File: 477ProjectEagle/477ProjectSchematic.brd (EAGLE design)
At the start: 100 x 80 mm, 49 parts, among them Q1 AO4419, X10 22-23-2041, X9 22-23-2041

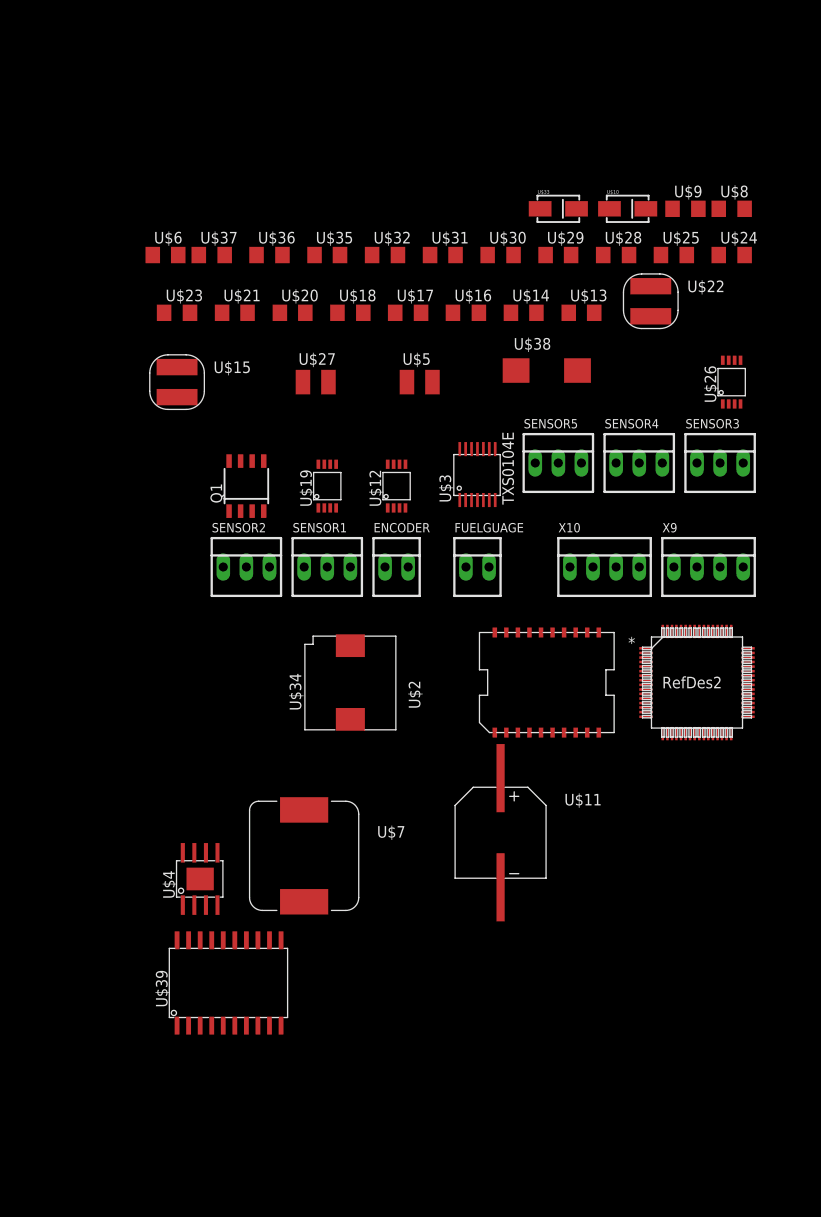
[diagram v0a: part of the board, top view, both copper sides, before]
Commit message: Updated micro code and small schematic fix
Added ADC code to micro project. The code initializes adc to capture
data from all 5 sensors the interrupt when done.
Also added decoupling caps to the ADC input lines.
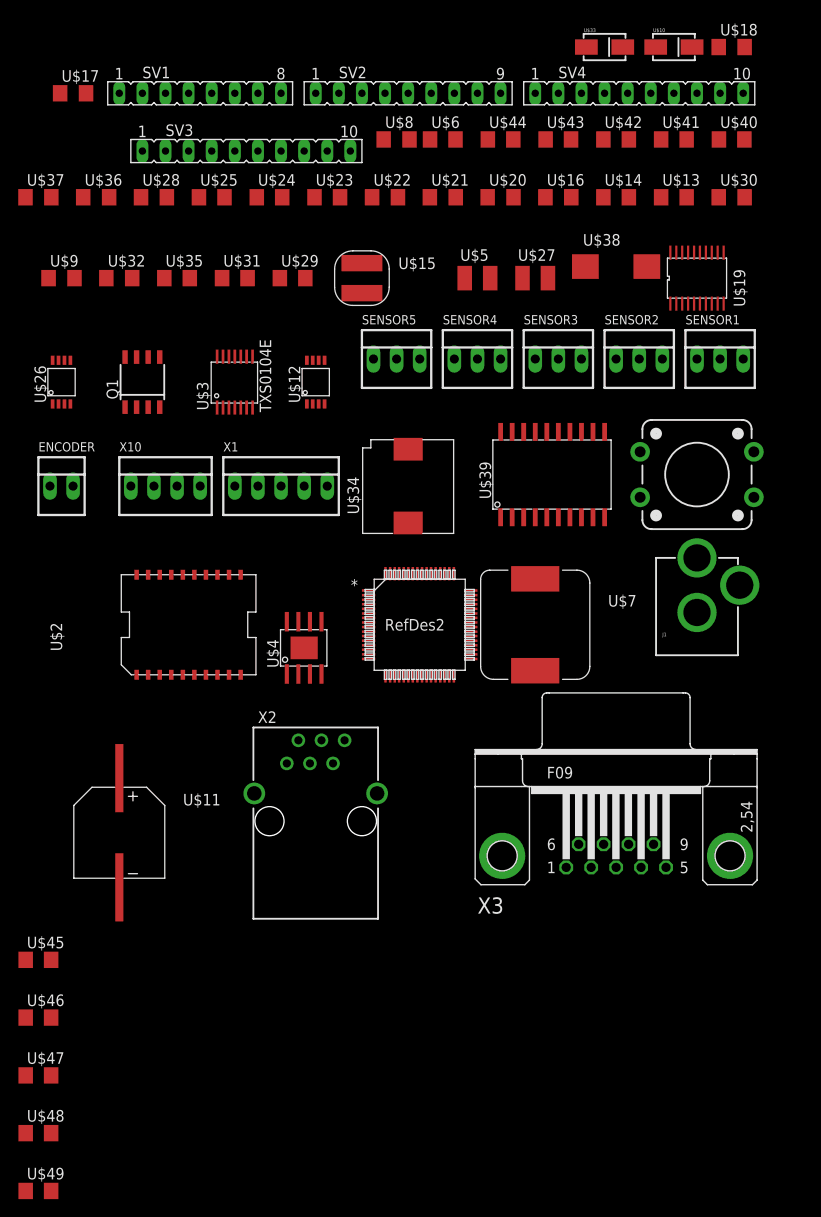
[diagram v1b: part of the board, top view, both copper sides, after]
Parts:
- removed FUELGUAGE: 22-23-2021, con-molex:22-23-2021
- removed X9: 22-23-2041, con-molex:22-23-2041
- added J1: POWER_JACKPTH, SparkFun-Connectors:POWER_JACK_PTH
- added SV1: (no value), con-lsta:FE08
- added SV2: (no value), con-lsta:FE09
- added SV3, SV4: (no value), con-lsta:FE10
- added SW_1: RESET_BUTTON, MinotaurParts:TACTILE-PTH-12MM
- added U$40, U$41, U$42, U$43, U$44, U$45, U$46, U$47, U$48, U$49: 10uF, MinotaurParts:C1206
- added X1: 22-23-2051, con-molex:22-23-2051
- added X2: XRJK-S-01-6-6-0-2G2-NO, con-xmultiple:XRJK-S-01-6-6-0-2G2-NO
- added X3: (no value), con-subd:F09HP
- U$11: value APXA100ARA271MJ80G -> 270uF
- U$13: value (none) -> 10uF
- U$14: value (none) -> 22uF
- U$15: value SDR0403 -> 2.2uH
- U$16: value (none) -> 100k
- U$19: value TPS62160 -> TXB0108; device MinotaurParts:MSOP-8 -> MinotaurParts:TXB0108
- U$20: value (none) -> 10k; device MinotaurParts:C1206 -> MinotaurParts:R1206
- U$21: value (none) -> 1k; device MinotaurParts:C1206 -> MinotaurParts:R1206
- U$22: value SDR0403 -> 5k; device MinotaurParts:SDR0403 -> MinotaurParts:R1206
- U$23, U$24, U$25: value (none) -> 10uF; device MinotaurParts:R1206 -> MinotaurParts:C1206
- U$27, U$5: value C-US-1210 -> 10uF
- U$28: value (none) -> 110k
- U$29: value (none) -> 740nF
- U$30: value (none) -> 2.55k
- U$31: value (none) -> 1.0nF
- U$32: value (none) -> 0.020
- U$34: value (none) -> 4.7uH
- U$35: value (none) -> 3.9nF
- U$36: value (none) -> 12k
- U$37: value (none) -> 1.4k
- U$38: value T495D336K025ATE090 -> 33uF
- U$6: value (none) -> 10nF
- U$7: value SRR1210 -> 12uH
- U$8: value (none) -> 10k
- U$9: value (none) -> 2.05k
- moved U$26 73.7 mm to (-90.2, 59.7)
- moved U$9 69.0 mm to (-90.2, 71.1)
- moved U$39 66.2 mm to (-35.6, 49.5)
- moved U$28 51.2 mm to (-80.0, 80.0)
- moved U$24 51.2 mm to (-67.3, 80.0)
- moved U$25 51.2 mm to (-73.7, 80.0)
- moved U$18 51.1 mm to (-16.5, 96.5)
- moved X10 49.1 mm to (-78.7, 48.3)
- moved SENSOR1 48.9 mm to (-17.8, 62.2)
- moved SENSOR2 48.9 mm to (-26.7, 62.2)
- moved U$19 46.6 mm to (-20.3, 71.1)
- moved U$17 44.0 mm to (-88.9, 91.4)
- moved U$11 41.9 mm to (-83.8, 10.2)
- moved U$2 39.9 mm to (-76.2, 33.0)
- moved ENCODER 37.9 mm to (-90.2, 48.3)
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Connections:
- net N$34 renamed +12V
- new net +3V3: U$1.10, U$1.26, U$1.38, U$19.VCCA, U$20.2, U$22.2, U$23.1, U$24.1, U$25.1, U$3.1, U$41.1, U$44.1, X1.2, X2.2
- new net +5V: SENSOR1.3, SENSOR2.3, SENSOR3.3, SENSOR4.3, SENSOR5.3, U$1.19, U$12.6, U$14.1, U$15.B, U$16.1, U$17.1, U$19.VCCB, U$3.14, U$39.VCC, U$40.1, U$42.1, U$43.1
- new net +7V: U$11.+, U$2.VS, U$7.B, U$8.2
- new net GND: J1.GND, J1.GNDBREAK, SENSOR1.2, SENSOR2.2, SENSOR3.2, SENSOR4.2, SENSOR5.2, SW_1.1, U$1.20, U$1.25, U$1.41, U$1.9, U$10.-, U$11.-, U$12.1, U$12.4, U$13.2, U$14.2, U$18.2, U$19.GND, U$2.GND, U$2.GND1, U$2.GND2, U$2.GND3, U$2.VSS, U$23.2, U$24.2, U$25.2, U$26.4, U$27.2, U$3.7, U$33.-, U$37.1, U$38.-, U$39.GND, U$39.GND2, U$4.6, U$4.PAD, U$40.2, U$41.2, U$42.2, U$43.2, U$44.2, U$45.2, U$46.2, U$47.2, U$48.2, U$49.2, U$5.2, U$9.1, X1.1, X3.1
- new net N$10: SV1.7, U$1.2
- new net N$11: SV1.6, U$1.3
- new net N$13: U$1.36
- new net N$14: U$1.15, X2.5
- new net N$15: U$1.64, U$19.A1
- new net N$16: U$10.+, U$4.8, U$6.1, U$7.A
- new net N$29: U$1.62, U$19.A3
- new net N$34: U$1.50, U$19.A5
- new net N$39: U$19.B1, U$2.IN1
- new net N$41: U$19.B4, U$2.IN4
- new net N$42: U$19.B2, U$2.IN2
- new net N$43: U$19.B3, U$2.IN3
- new net N$49: U$19.B8, U$39.T1IN
- new net N$53: U$39.T1OUT, X3.2
- new net N$56: U$19.OE, U$20.1
- new net N$57: U$1.29
- new net N$58: U$1.7, U$21.2, U$22.1, X2.1
- new net N$59: U$1.40
- new net N$6: SV1.8, U$1.1
- new net N$60: SW_1.3, U$21.1
- new net N$61: SV2.4, U$1.28
- new net N$62: U$1.27
- new net N$63: U$1.24
- new net N$64: SV2.7, U$1.23
- new net N$65: U$1.21
- new net N$66: U$1.18
- new net N$67: SV4.10, U$1.35
- new net N$68: U$1.39
- new net N$69: U$1.42
- new net N$7: U$1.16, X2.4
- new net N$70: SV4.6, U$1.43
- new net N$71: SV4.5, U$1.44
- new net N$72: SV4.4, U$1.45
- new net N$73: SV4.3, U$1.46
- new net N$74: U$1.47
- new net N$75: U$1.48
- new net N$76: SV3.1, U$1.60
- new net N$77: SV3.2
- new net N$78: SV3.3
- new net N$79: SV3.4
- new net N$80: SV3.5
- new net N$81: SV3.6
- new net N$82: SV3.7, U$1.54
- new net N$83: SV3.8, U$1.53
- new net N$84: SV3.9, U$1.52
- new net N$85: SV3.10
- new net N$86: X2.3
- new net N$87: U$39.R1IN, X3.3
- new net SCL: ENCODER.1, X1.4
- new net SDA: ENCODER.2, X1.3
- new net V+: J1.PWR, U$12.2, U$12.3, U$13.1, U$26.8, U$27.1, U$28.2, U$29.1, U$30.2, U$31.1, U$32.2, U$4.7, U$5.1
- net N$1: now also U$49.1
- net N$17: now also U$1.63, U$19.A2; no longer U$2.IN4
- net N$19: now also U$2.OUT2
- net N$2: now also U$48.1
- net N$20: now also X10.3; no longer X9.1
- net N$21: now also U$2.OUT3, X10.4; no longer X9.2
- net N$22: now also U$1.30
- net N$23: now also SV1.5, U$1.4; no longer ENCODER.1, FUELGUAGE.1
- net N$24: now also SV1.4, U$1.5; no longer ENCODER.2, FUELGUAGE.2
- net N$26: now also SV1.3, U$1.6; no longer U$10.+, U$12.2, U$12.3, U$13.1, U$19.2, U$19.3, U$20.1, U$26.8, U$27.1, U$28.2, U$29.1, U$30.2, U$31.1, U$32.2, U$4.8, U$6.1, U$7.B
- net N$27: now also SV1.2, U$1.8; no longer U$11.+, U$7.A, U$8.2, X9.3
- net N$3: now also U$47.1
- net N$30: now also SV1.1, U$1.17; no longer U$4.7, U$5.1
- net N$31: now also U$1.32; no longer U$1.60
- net N$32: now also U$1.61, U$19.A4; no longer SENSOR1.2, SENSOR2.2, SENSOR3.2, SENSOR4.2, SENSOR5.2, U$1.41, U$1.9, U$10.-, U$11.-, U$12.1, U$12.4, U$13.2, U$14.2, U$18.2, U$19.1, U$19.4, U$20.2, U$21.2, U$25.2, U$26.4, U$27.2, U$33.-, U$37.1, U$38.-, U$4.6, U$4.PAD, U$5.2, U$9.1, X10.4, X9.4
- net N$38: now also U$1.49, U$19.A6; no longer SENSOR1.3, SENSOR2.3, SENSOR3.3, SENSOR4.3, SENSOR5.3, U$12.6, U$14.1, U$15.B, U$16.1, U$17.1, U$3.14, U$39.VCC
- net N$4: now also U$46.1
- net N$44: now also U$19.B5, U$2.ENA; no longer U$19.7, U$22.A
- net N$45: now also U$19.B6, U$2.ENB; no longer U$19.8, U$23.2
- net N$46: now also U$1.31; no longer U$1.10, U$1.26, U$19.6, U$21.1, U$22.B, U$23.1, U$24.1, U$3.1
- net N$47: now also U$19.B7, U$39.R1OUT; no longer U$19.5, U$24.2, U$25.1
- net N$5: now also U$1.22, U$45.1
- net N$8: now also U$19.A7; no longer U$39.R1OUT
- net N$9: now also U$1.33, U$19.A8; no longer U$39.T1IN

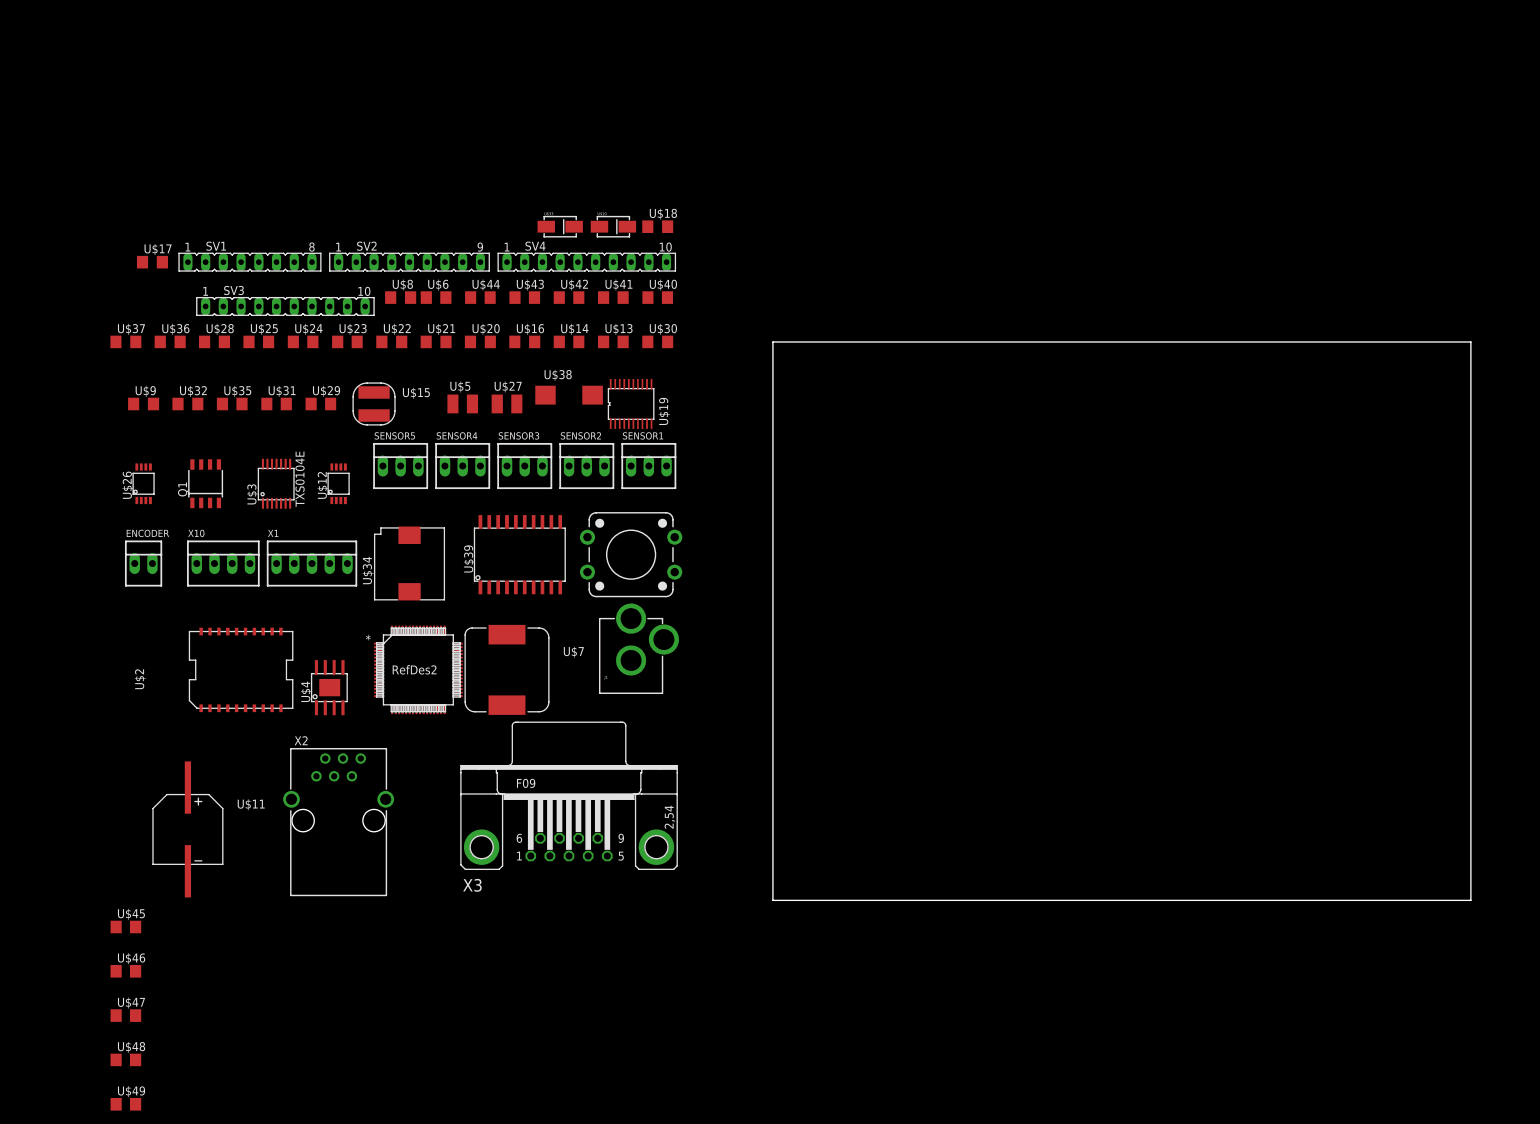
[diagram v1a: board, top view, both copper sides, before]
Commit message: started main PCB layout - 12V supply done
Started the PCB layout. Got the 12 volt power supply circuit done. We
only have the Light version of eagle so I couldn't actually make the PCB
the right size.
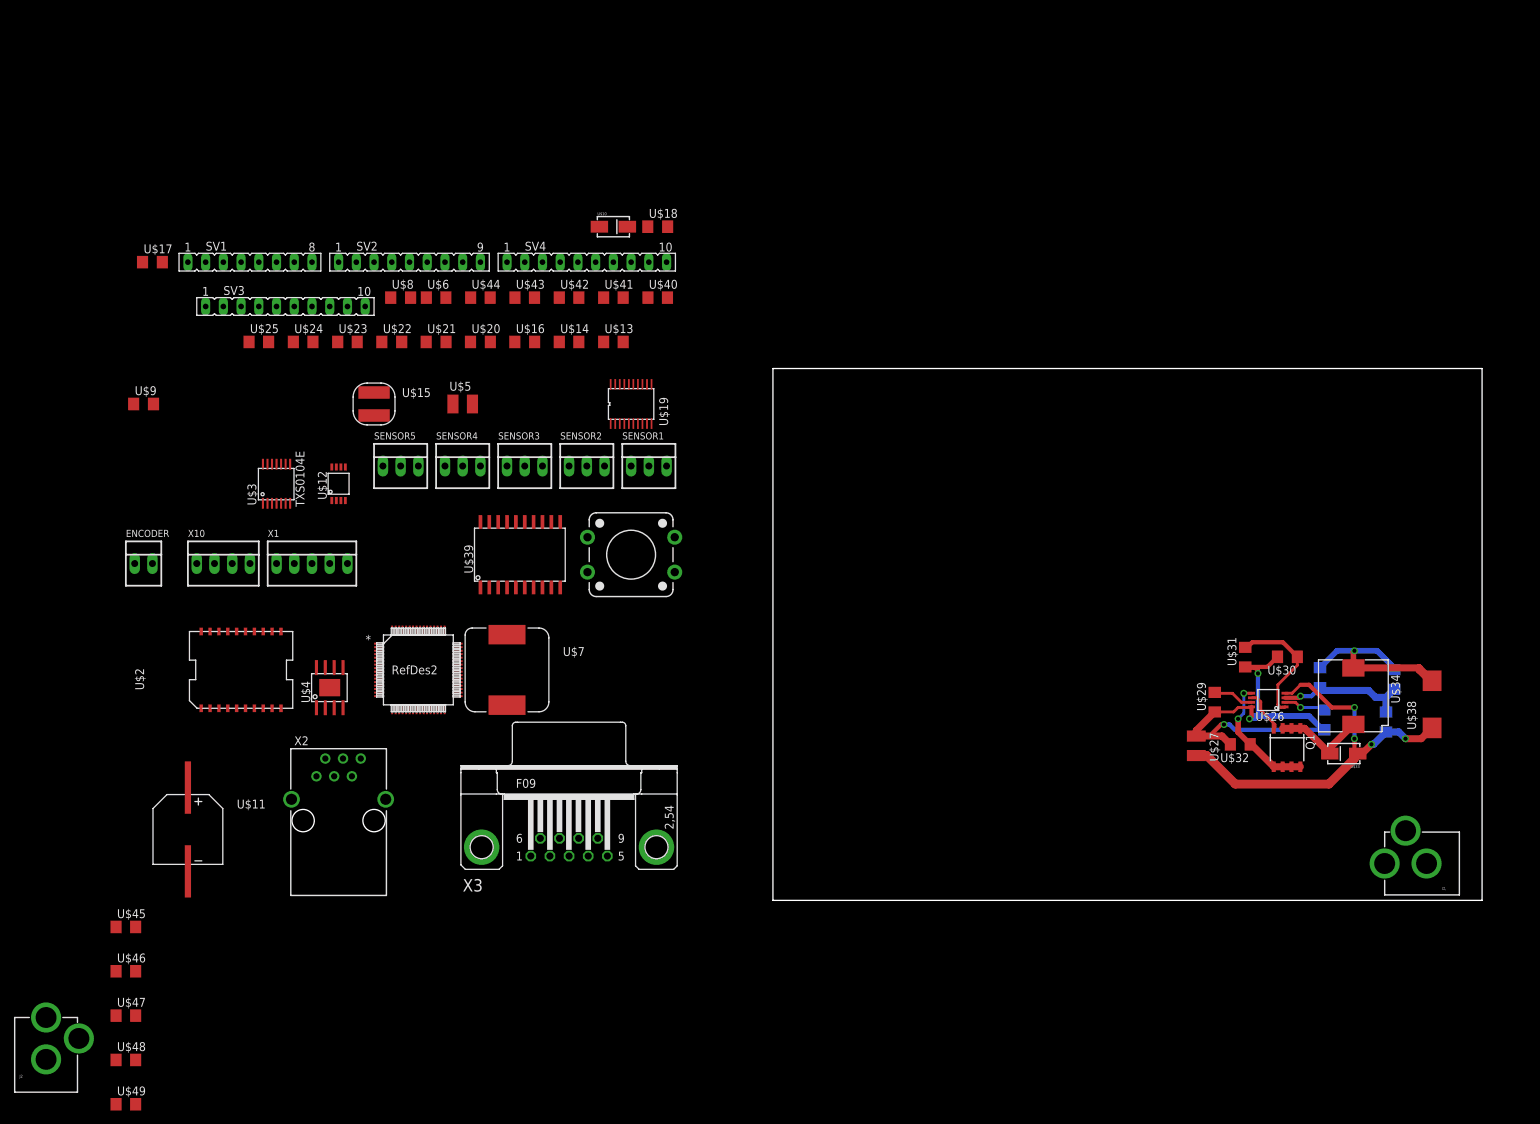
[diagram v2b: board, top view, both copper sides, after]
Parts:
- added J2: POWER_JACK_12VOUT, SparkFun-Connectors:POWER_JACK_PTH
- J1: value POWER_JACKPTH -> POWER_JACK_BAT
- moved U$37 188.6 mm to (87.8, 25.6), flipped to the bottom, turned to 90 degrees
- moved U$36 171.6 mm to (78.4, 31.9), flipped to the bottom, turned to 90 degrees
- moved U$35 171.1 mm to (89.0, 31.6), flipped to the bottom, turned to 270 degrees
- moved U$28 168.0 mm to (79.0, 25.9), flipped to the bottom, turned to 270 degrees
- moved U$26 164.1 mm to (71.0, 28.7), turned to 90 degrees
- moved Q1 159.5 mm to (73.7, 21.9), turned to 180 degrees
- moved U$32 158.5 mm to (67.0, 22.4), turned to 180 degrees
- moved U$31 143.4 mm to (67.7, 34.8), turned to 90 degrees
- moved U$34 136.6 mm to (83.2, 29.3), turned to 180 degrees
- moved U$33 135.3 mm to (81.8, 21.0), turned to 180 degrees
- moved U$29 135.0 mm to (63.3, 28.4), turned to 90 degrees
- moved U$38 131.3 mm to (94.4, 28.1), turned to 90 degrees
- moved J1 123.5 mm to (101.3, 5.28), turned to 90 degrees
- moved U$27 110.2 mm to (60.7, 22.1), turned to 270 degrees
- moved U$30 100.9 mm to (73.7, 34.9), turned to 180 degrees
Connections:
- net +12V: now also J2.PWR
- net GND: now also J2.GND, J2.GNDBREAK
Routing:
- net V+: track 0.00 -> 62.0 mm, vias 0 -> 3
- net GND: track 0.00 -> 59.5 mm, vias 0 -> 4
- net +12V: track 0.00 -> 30.2 mm, vias 0 -> 1
- net N$35: track 0.00 -> 19.4 mm, vias 0 -> 1
- net N$54: track 0.00 -> 18.0 mm, vias 0 -> 2
- net N$52: track 0.00 -> 17.9 mm
- net N$33: track 0.00 -> 13.8 mm
- net N$55: track 0.00 -> 6.29 mm
- net N$48: track 0.00 -> 6.08 mm, vias 0 -> 1
- net N$51: track 0.00 -> 5.86 mm
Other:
- board size 100 x 80 mm -> 101.6 x 76.2 mm
